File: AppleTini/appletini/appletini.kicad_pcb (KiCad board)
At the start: 4 copper layers, 114.3 x 66.7 mm, 30 parts, among them J1 Conn_02x25_Counter_Clockwise, Q1 DMG2305UX-7, SW1 SW_Push, U1 74LS245, U2 74LS245, U3 74LS245, U4 74LS245, U5 74LS245, U6 74LS07, U7 Pico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

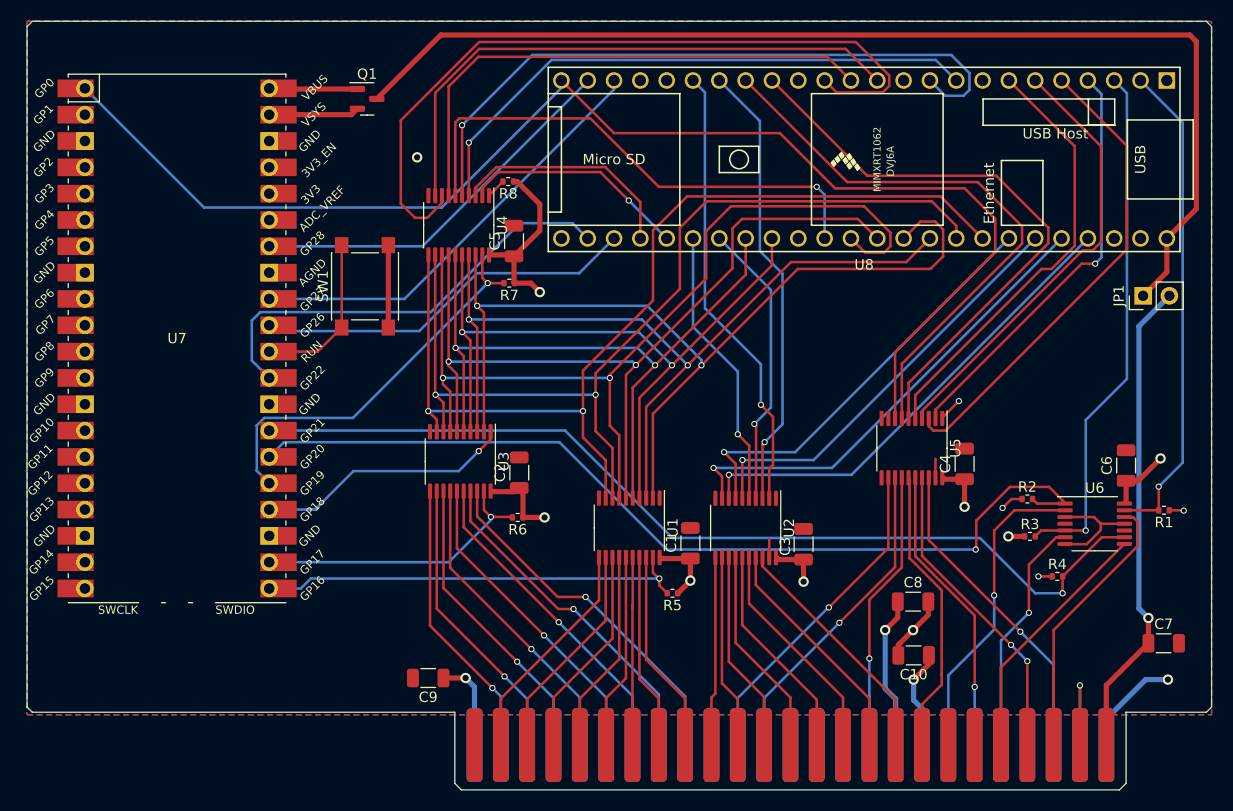
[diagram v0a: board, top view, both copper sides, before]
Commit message: Increased via spacing
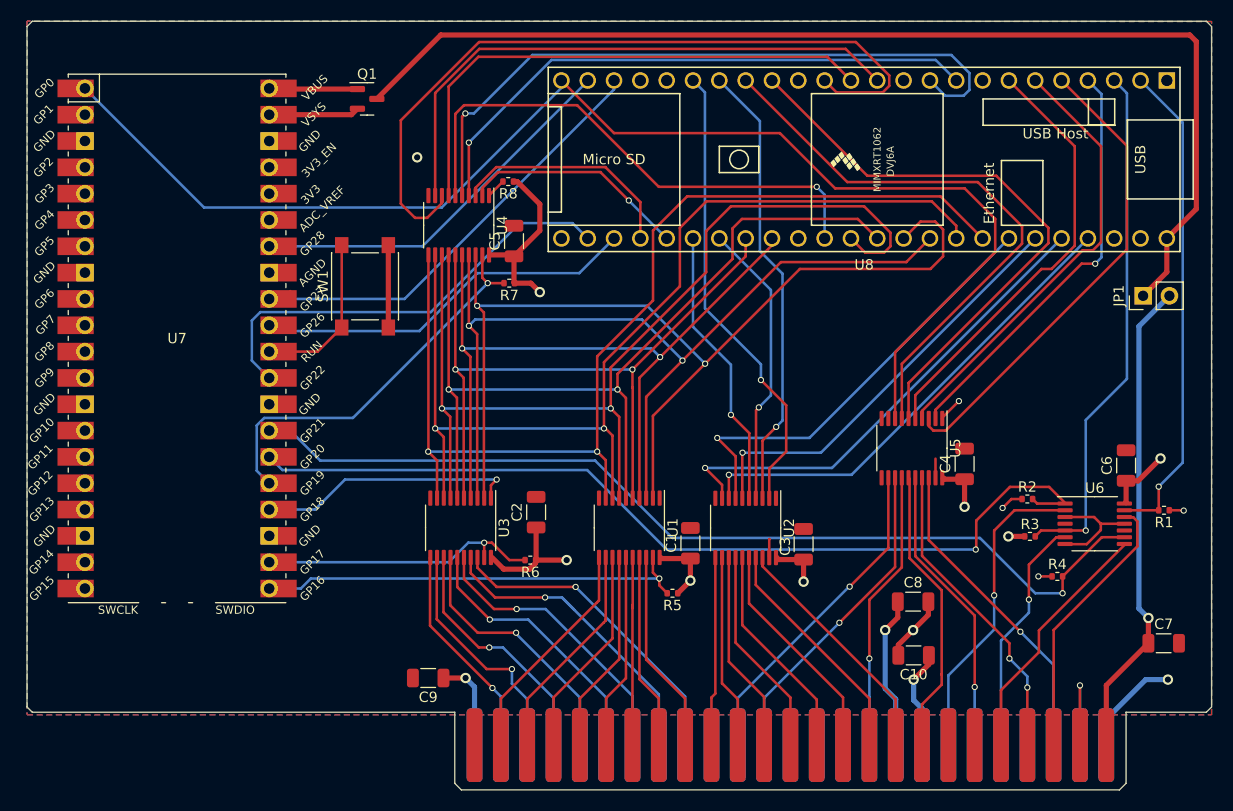
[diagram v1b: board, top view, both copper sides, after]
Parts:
- moved U3 6.40 mm to (118.0, 115.6)
- moved R6 4.29 mm to (124.8, 118.7)
- moved C2 4.14 mm to (125.3, 114.0)
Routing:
- net /Transceivers/ALO_D1: track 92.9 -> 99.6 mm
- net /Transceivers/ALO_D0: track 96.7 -> 103.4 mm
- net /Transceivers/ALO_D6: track 83.3 -> 89.8 mm
- net /Transceivers/ALO_D2: track 89.3 -> 95.8 mm
- net /BUS_D0: track 27.3 -> 21.0 mm
- net /Transceivers/ALO_D7: track 91.5 -> 97.8 mm
- net /Transceivers/ALO_D3: track 81.0 -> 86.2 mm
- net /BUS_D2: track 28.9 -> 23.9 mm
- net /BUS_D1: track 28.1 -> 23.2 mm
- net /Transceivers/ALO_D5: track 69.3 -> 73.6 mm
- net /BUS_D4: track 30.5 -> 26.2 mm
- net /BUS_D3: track 29.7 -> 25.5 mm
- net /Transceivers/ALO_D4: track 66.9 -> 70.5 mm
- net /BUS_D7: track 34.4 -> 30.9 mm
- net /BUS_D5: track 31.3 -> 27.8 mm
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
